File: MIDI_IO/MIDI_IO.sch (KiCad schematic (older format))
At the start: 21 parts, among them J1 Conn_01x04, U1 6N138

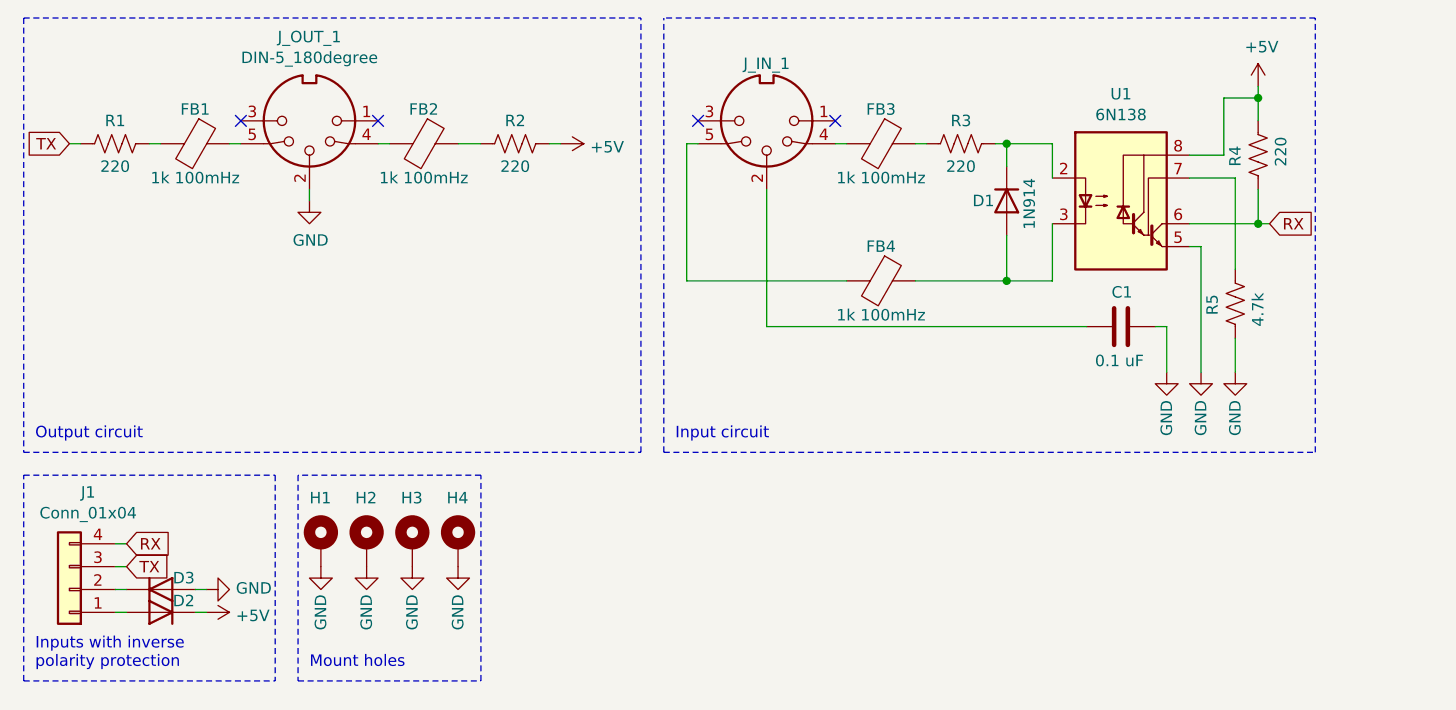
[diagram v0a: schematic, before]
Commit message: Improves MIDI shield
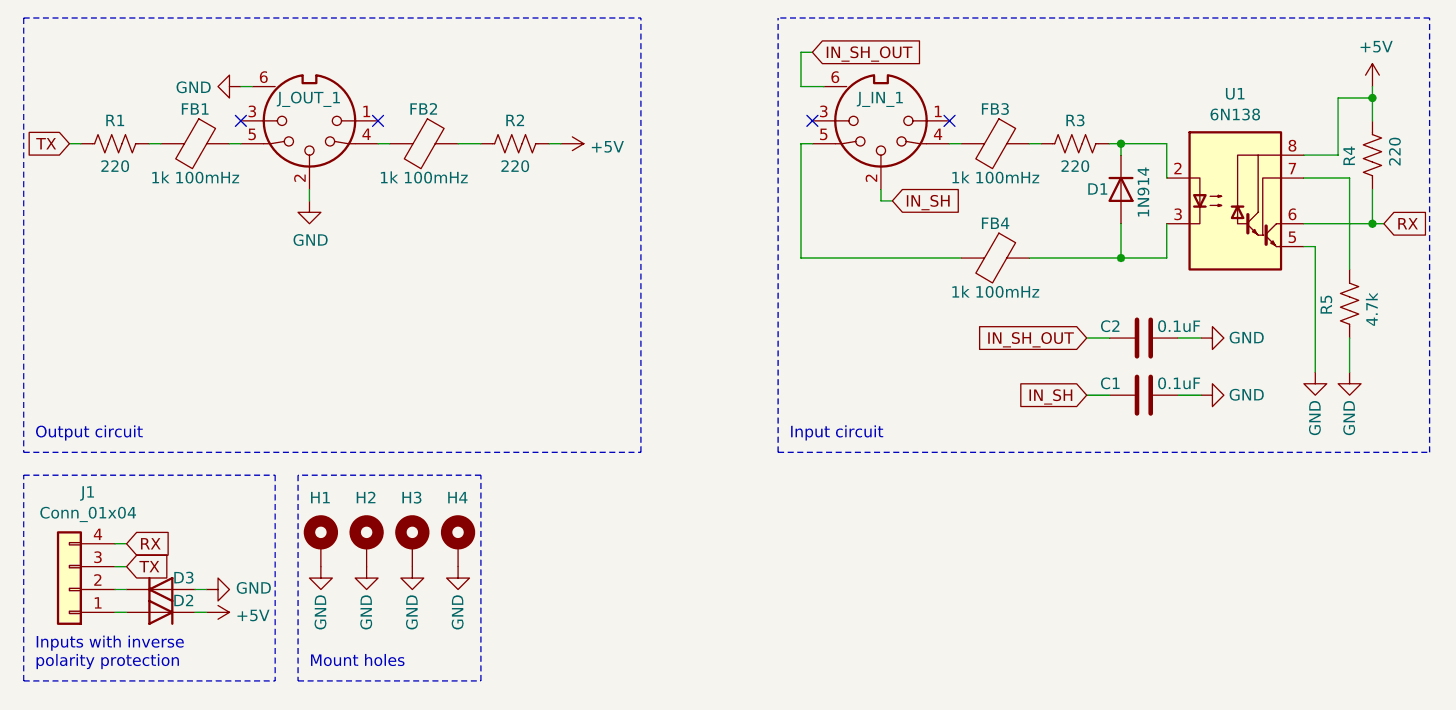
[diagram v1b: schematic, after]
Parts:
- removed J_IN_1, J_OUT_1: DIN-5_180degree, w_conn_av:din-5, symbol Connector:DIN-5_180degree
- added C2: 0.1uF, Capacitor_SMD:C_0603_1608Metric, symbol Device:C
- added J_IN_1, J_OUT_1: DIN-5_180degree_JS, MIDI_IO:din-5-shielded, symbol din-5_180degree_jack_shield:DIN-5_180degree_JS
- C1: value 0.1 uF -> 0.1uF
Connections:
- net GND: now also C2.2, J_OUT_1.2, J_OUT_1.6
- net at FB2.2: now also J_OUT_1.4
- net at FB1.1: now also J_OUT_1.5
- net IN_SH: now reaches C1.1
- net IN_SH: now also J_IN_1.2
- net at FB3.2: now also J_IN_1.4
- net at FB4.2: now also J_IN_1.5
- new net IN_SH_OUT: C2.1, J_IN_1.6
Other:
- moved on the sheet: C1, D1, FB3, FB4, R3, R4, R5, U1

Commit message: Updates MIDI-IO board to a last state
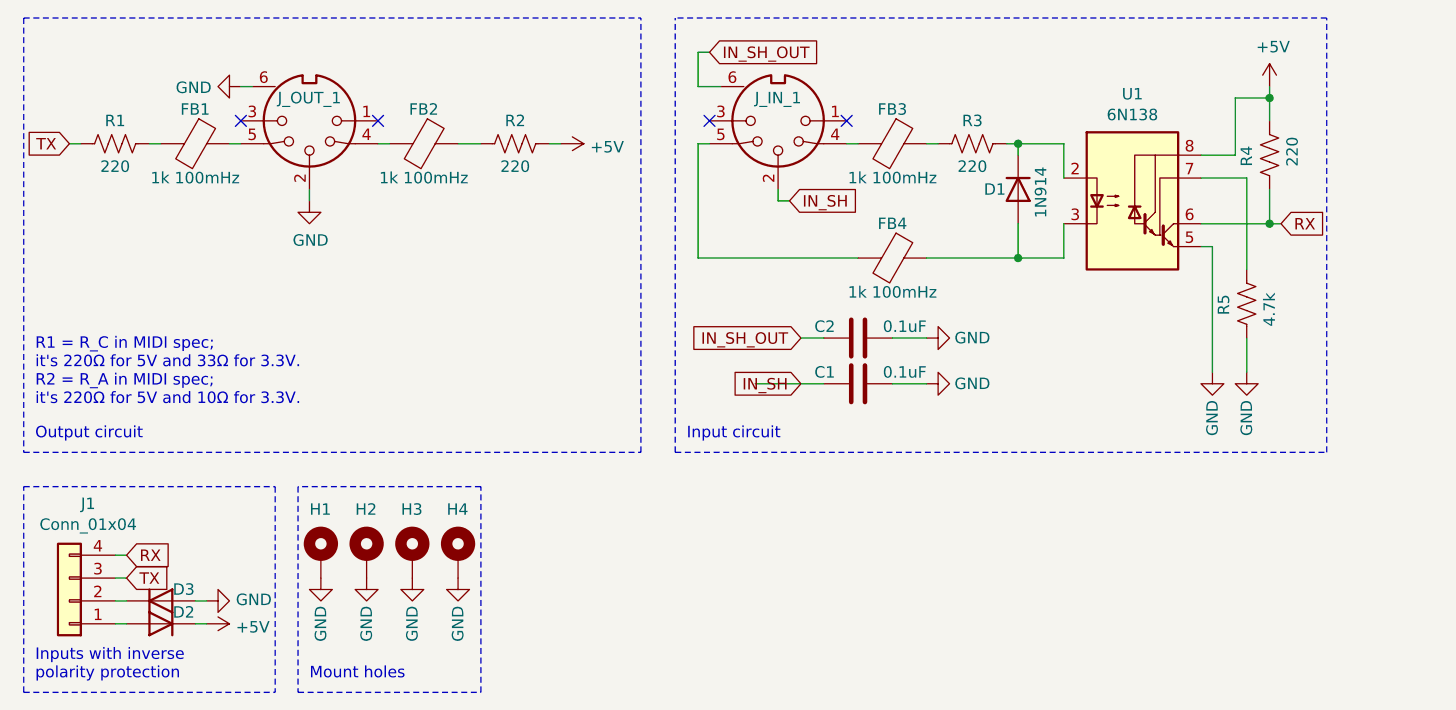
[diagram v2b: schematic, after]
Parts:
- D2, D3: footprint Diode_SMD:D_0402_1005Metric -> Diode_SMD:D_0603_1608Metric
- FB1, FB2, FB3, FB4: footprint Inductor_SMD:L_0402_1005Metric -> Inductor_SMD:L_0603_1608Metric
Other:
- note added: "R1 = R_C in MIDI spec;\nit's 220Ω for 5V and 33Ω for 3.3V.\nR2 = R_A in MIDI spec;\nit's 220Ω for 5V and 10Ω for 3.3V."
- moved on the sheet: C1, C2, D1, D2, D3, FB3, FB4, H1, H2, H3, H4, J1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
